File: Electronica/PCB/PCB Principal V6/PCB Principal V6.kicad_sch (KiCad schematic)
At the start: 19 parts, among them J1 Conexion Sensores, J12 TP, J2 Power Monster, J3 On/Off General, J4 Power Input 2, J5 IDC Placa Botones, J6 Power Input 1, J7 Conn_01x01_Pin, J8 Conn_01x01_Pin, SW1 On/Off Motores

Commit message: ,
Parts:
- LM1: footprint Step Down:LM2596_correctedMeas -> StepDown:StepDown
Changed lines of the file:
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@@
 		)
 		(instances
-			(project "PCB Principal V5"
+			(project "PCB Principal V6"
 				(path "/feeeb2cb-e374-40f4-b9c7-40ed321ecf02"
 					(reference "#PWR022")
@@
 		)
 		(instances
-			(project "PCB Principal V5"
+			(project "PCB Principal V6"
 				(path "/feeeb2cb-e374-40f4-b9c7-40ed321ecf02"
 					(reference "#PWR021")
@@
 		)
 		(instances
-			(project "PCB Principal V5"
+			(project "PCB Principal V6"
 				(path "/feeeb2cb-e374-40f4-b9c7-40ed321ecf02"
 					(reference "#PWR01")
@@
 		)
 		(instances
-			(project "PCB Principal V5"
+			(project "PCB Principal V6"
 				(path "/feeeb2cb-e374-40f4-b9c7-40ed321ecf02"
 					(reference "#PWR013")
@@
 		)
 		(instances
-			(project "PCB Principal V5"
+			(project "PCB Principal V6"
 				(path "/feeeb2cb-e374-40f4-b9c7-40ed321ecf02"
 					(reference "#PWR012")
@@
 		)
 		(instances
-			(project "PCB Principal V5"
+			(project "PCB Principal V6"
 				(path "/feeeb2cb-e374-40f4-b9c7-40ed321ecf02"
 					(reference "#PWR05")
@@
 		)
 		(instances
-			(project "PCB Principal V5"
+			(project "PCB Principal V6"
 				(path "/feeeb2cb-e374-40f4-b9c7-40ed321ecf02"
 					(reference "J1")
@@
 		)
 		(instances
-			(project "PCB Principal V5"
+			(project "PCB Principal V6"
 				(path "/feeeb2cb-e374-40f4-b9c7-40ed321ecf02"
 					(reference "D1")
@@
 		)
 		(instances
-			(project "PCB Principal V5"
+			(project "PCB Principal V6"
 				(path "/feeeb2cb-e374-40f4-b9c7-40ed321ecf02"
 					(reference "#PWR019")
@@
 		)
 		(instances
-			(project "PCB Principal V5"
+			(project "PCB Principal V6"
 				(path "/feeeb2cb-e374-40f4-b9c7-40ed321ecf02"
 					(reference "J5")
@@
 		)
 		(instances
-			(project "PCB Principal V5"
+			(project "PCB Principal V6"
 				(path "/feeeb2cb-e374-40f4-b9c7-40ed321ecf02"
 					(reference "J3")
@@
 		)
 		(instances
-			(project "PCB Principal V5"
+			(project "PCB Principal V6"
 				(path "/feeeb2cb-e374-40f4-b9c7-40ed321ecf02"
 					(reference "#PWR017")
@@
 		)
 		(instances
-			(project "PCB Principal V5"
+			(project "PCB Principal V6"
 				(path "/feeeb2cb-e374-40f4-b9c7-40ed321ecf02"
 					(reference "#PWR07")
@@
 		)
 		(instances
-			(project "PCB Principal V5"
+			(project "PCB Principal V6"
 				(path "/feeeb2cb-e374-40f4-b9c7-40ed321ecf02"
 					(reference "D4")
@@
 			)
 		)
-		(property "Footprint" "Step Down:LM2596_correctedMeas"
+		(property "Footprint" "StepDown:StepDown"
 			(at 119.38 123.19 0)
 			(effects
@@
 		)
 		(instances
-			(project "PCB Principal V5"
+			(project "PCB Principal V6"
 				(path "/feeeb2cb-e374-40f4-b9c7-40ed321ecf02"
 					(reference "LM1")
@@
 		)
 		(instances
-			(project "PCB Principal V5"
+			(project "PCB Principal V6"
 				(path "/feeeb2cb-e374-40f4-b9c7-40ed321ecf02"
 					(reference "SW1")
@@
 		)
 		(instances
-			(project "PCB Principal V5"
+			(project "PCB Principal V6"
 				(path "/feeeb2cb-e374-40f4-b9c7-40ed321ecf02"
 					(reference "#PWR02")
@@
 		)
 		(instances
-			(project "PCB Principal V5"
+			(project "PCB Principal V6"
 				(path "/feeeb2cb-e374-40f4-b9c7-40ed321ecf02"
 					(reference "#PWR015")
@@
 		)
 		(instances
-			(project "PCB Principal V5"
+			(project "PCB Principal V6"
 				(path "/feeeb2cb-e374-40f4-b9c7-40ed321ecf02"
 					(reference "D2")
@@
 		)
 		(instances
-			(project "PCB Principal V5"
+			(project "PCB Principal V6"
 				(path "/feeeb2cb-e374-40f4-b9c7-40ed321ecf02"
 					(reference "R2")
@@
 		)
 		(instances
-			(project "PCB Principal V5"
+			(project "PCB Principal V6"
 				(path "/feeeb2cb-e374-40f4-b9c7-40ed321ecf02"
 					(reference "J7")
@@
 		)
 		(instances
-			(project "PCB Principal V5"
+			(project "PCB Principal V6"
 				(path "/feeeb2cb-e374-40f4-b9c7-40ed321ecf02"
 					(reference "#PWR011")
@@
 		)
 		(instances
-			(project "PCB Principal V5"
+			(project "PCB Principal V6"
 				(path "/feeeb2cb-e374-40f4-b9c7-40ed321ecf02"
 					(reference "D3")
@@
 		)
 		(instances
-			(project "PCB Principal V5"
+			(project "PCB Principal V6"
 				(path "/feeeb2cb-e374-40f4-b9c7-40ed321ecf02"
 					(reference "#PWR08")
@@
 		)
 		(instances
-			(project "PCB Principal V5"
+			(project "PCB Principal V6"
 				(path "/feeeb2cb-e374-40f4-b9c7-40ed321ecf02"
 					(reference "#PWR016")
@@
 		)
 		(instances
-			(project "PCB Principal V5"
+			(project "PCB Principal V6"
 				(path "/feeeb2cb-e374-40f4-b9c7-40ed321ecf02"
 					(reference "#PWR020")
@@
 		)
 		(instances
-			(project "PCB Principal V5"
+			(project "PCB Principal V6"
 				(path "/feeeb2cb-e374-40f4-b9c7-40ed321ecf02"
 					(reference "R1")
@@
 		)
 		(instances
-			(project "PCB Principal V5"
+			(project "PCB Principal V6"
 				(path "/feeeb2cb-e374-40f4-b9c7-40ed321ecf02"
 					(reference "J6")
@@
 		)
 		(instances
-			(project "PCB Principal V5"
+			(project "PCB Principal V6"
 				(path "/feeeb2cb-e374-40f4-b9c7-40ed321ecf02"
 					(reference "#PWR04")
@@
 		)
 		(instances
-			(project "PCB Principal V5"
+			(project "PCB Principal V6"
 				(path "/feeeb2cb-e374-40f4-b9c7-40ed321ecf02"
 					(reference "#PWR03")
@@
 		)
 		(instances
-			(project "PCB Principal V5"
+			(project "PCB Principal V6"
 				(path "/feeeb2cb-e374-40f4-b9c7-40ed321ecf02"
 					(reference "J2")
@@
 		)
 		(instances
-			(project "PCB Principal V5"
+			(project "PCB Principal V6"
 				(path "/feeeb2cb-e374-40f4-b9c7-40ed321ecf02"
 					(reference "J8")
@@
 		)
 		(instances
-			(project "PCB Principal V5"
+			(project "PCB Principal V6"
 				(path "/feeeb2cb-e374-40f4-b9c7-40ed321ecf02"
 					(reference "#PWR09")
@@
 		)
 		(instances
-			(project "PCB Principal V5"
+			(project "PCB Principal V6"
 				(path "/feeeb2cb-e374-40f4-b9c7-40ed321ecf02"
 					(reference "J4")
@@
 		)
 		(instances
-			(project "PCB Principal V5"
+			(project "PCB Principal V6"
 				(path "/feeeb2cb-e374-40f4-b9c7-40ed321ecf02"
 					(reference "A1")
@@
 		)
 		(instances
-			(project "PCB Principal V5"
+			(project "PCB Principal V6"
 				(path "/feeeb2cb-e374-40f4-b9c7-40ed321ecf02"
 					(reference "J12")
@@
 		)
 		(instances
-			(project "PCB Principal V5"
+			(project "PCB Principal V6"
 				(path "/feeeb2cb-e374-40f4-b9c7-40ed321ecf02"
 					(reference "#PWR010")
@@
 		)
 		(instances
-			(project "PCB Principal V5"
+			(project "PCB Principal V6"
 				(path "/feeeb2cb-e374-40f4-b9c7-40ed321ecf02"
 					(reference "A2")
@@
 		)
 		(instances
-			(project "PCB Principal V5"
+			(project "PCB Principal V6"
 				(path "/feeeb2cb-e374-40f4-b9c7-40ed321ecf02"
 					(reference "#PWR014")
@@
 		)
 		(instances
-			(project "PCB Principal V5"
+			(project "PCB Principal V6"
 				(path "/feeeb2cb-e374-40f4-b9c7-40ed321ecf02"
 					(reference "#PWR018")
@@
 		)
 		(instances
-			(project "PCB Principal V5"
+			(project "PCB Principal V6"
 				(path "/feeeb2cb-e374-40f4-b9c7-40ed321ecf02"
 					(reference "#PWR06")

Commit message: PCB CHERNIAK TERMINAR
TONTO EL QUE LEE
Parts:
- removed J7, J8: Conn_01x01_Pin, Connector_PinHeader_2.54mm:PinHeader_1x01_P2.54mm_Vertical, symbol Connector:Conn_01x01_Pin

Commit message: pcb terminar?
TONTO EL QUE LEE
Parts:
- removed J12: TP, Connector_PinHeader_2.54mm:PinHeader_1x05_P2.54mm_Vertical, symbol Connector_Generic:Conn_01x05
- added J10, J7, J8, J9: Conn_01x01, Connector_PinHeader_2.54mm:PinHeader_1x01_P2.54mm_Vertical, symbol Connector_Generic:Conn_01x01
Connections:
- net +5V: now also J9.1 (Pin_1)
- net GND: now also J10.1 (Pin_1)
- net PI+: now also J8.1 (Pin_1)
- net VNano: now also J7.1 (Pin_1)

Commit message: .
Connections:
- net CNY 1: now also A1.26 (A7); no longer A1.25 (A6)
- net CNY 2: now also A1.25 (A6); no longer A1.26 (A7)
- net ECHO 1: now also A1.11 (D8); no longer A1.14 (D11)
- net ECHO 2: now also J1.5 (Pin_5); no longer J1.3 (Pin_3)
- net LED2: now also A1.22 (A3); no longer A1.24 (A5)
- net LED4: now also A1.24 (A5); no longer A1.16 (D13)
- net TRIG 1: now also J1.3 (Pin_3); no longer J1.5 (Pin_5)
- net TRIG 2: now also A1.14 (D11); no longer A1.11 (D8)
- net TRIG 3: now also A1.16 (D13); no longer A1.22 (A3)

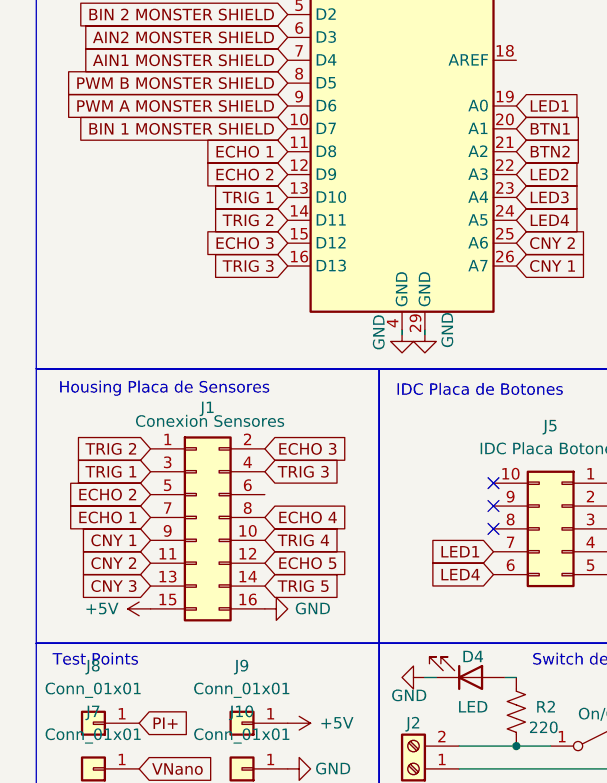
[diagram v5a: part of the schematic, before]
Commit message: Placa sensores y placa principar terminada
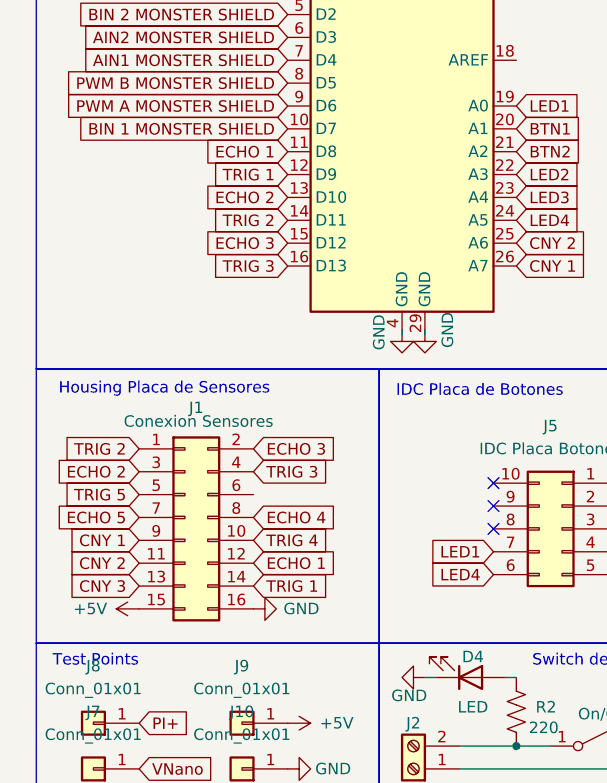
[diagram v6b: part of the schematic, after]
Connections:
- net ECHO 1: now also J1.12 (Pin_12); no longer J1.7 (Pin_7)
- net ECHO 2: now also A1.13 (D10), J1.3 (Pin_3); no longer A1.12 (D9), J1.5 (Pin_5)
- net ECHO 5: now also J1.7 (Pin_7); no longer J1.12 (Pin_12)
- net TRIG 1: now also A1.12 (D9), J1.14 (Pin_14); no longer A1.13 (D10), J1.3 (Pin_3)
- net TRIG 5: now also J1.5 (Pin_5); no longer J1.14 (Pin_14)

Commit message: PCB V6 ACTUALIZADA
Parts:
- added U1: 74HC595, 74HC595N_DIP16_:DIP16-2.54-20.32X5.84MM, symbol 74xx:74HC595
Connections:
- net +5V: now also U1.10 (~{SRCLR}), U1.16 (VCC)
- net BTN1: now also A1.23 (A4); no longer A1.20 (A1)
- net BTN2: now also A1.24 (A5); no longer A1.21 (A2)
- net CNY 1: now also A1.25 (A6); no longer A1.26 (A7)
- net CNY 2: now also A1.26 (A7); no longer A1.25 (A6)
- net ECHO 2: now also A1.12 (D9); no longer A1.13 (D10)
- net ECHO 3: now also A1.13 (D10); no longer A1.15 (D12)
- net ECHO 4: now also A1.20 (A1)
- net ECHO 5: now also A1.21 (A2)
- net GND: now also U1.13 (~{OE}), U1.8 (GND)
- net LED1: now also U1.6 (QG); no longer A1.19 (A0)
- net LED2: now also U1.4 (QE); no longer A1.22 (A3)
- net LED3: now also U1.15 (QA); no longer A1.23 (A4)
- net LED4: now also A1.22 (A3); no longer A1.24 (A5)
- net TRIG 1: now also U1.7 (QH); no longer A1.12 (D9)
- net TRIG 2: now also U1.1 (QB); no longer A1.14 (D11)
- net TRIG 3: now also U1.2 (QC); no longer A1.16 (D13)
- net TRIG 4: now also U1.5 (QF)
- net TRIG 5: now also U1.3 (QD)
- new net Clock: A1.16 (D13), U1.11 (SRCLK)
- new net Data: A1.14 (D11), U1.14 (SER)
- new net Latch: A1.15 (D12), U1.12 (RCLK)
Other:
- note added: "Arduino NANO"
- note added: "Monster Shield"
- note added: "Shift Register"
